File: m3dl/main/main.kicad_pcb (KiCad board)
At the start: 2 copper layers, 40 x 40 mm, 34 parts, among them IC1 STM32F405RxTx, IC2 MCP2562, J1 WEST TOP, J2 EAST TOP, J3 WEST BOT, J4 EAST BOT, J6 MICROUSB, J7 SOUTH TOP, P1 SWD_TC, U1 MICROSD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

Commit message: Finished Routing & Silk on all Boards
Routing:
- net (no net): vias 1 -> 0
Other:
- board text added: "C10"
- board text added: "C11"
- board text added: "C12"
- board text added: "C13"
- board text added: "C14"
- board text added: "C15"
- board text added: "C16"
- board text added: "C2"
- board text added: "C3"
- board text added: "C4"
- board text added: "C5"
- board text added: "C6"
- board text added: "C7"
- board text added: "C8"
- board text added: "C9"
- board text added: "R1"
- board text added: "R2"
- board text added: "R3"
- board text added: "R4"
- board text added: "R5"
- board text added: "R6"
- board text added: "R7"
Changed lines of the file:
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@@
     (area 79.725 77.094999 120.075001 120.075001)
     (thickness 1.6)
-    (drawings 2)
-    (tracks 632)
+    (drawings 24)
+    (tracks 631)
     (zones 0)
     (modules 34)
@@
     (34 B.Paste user hide)
     (35 F.Paste user hide)
-    (36 B.SilkS user hide)
-    (37 F.SilkS user hide)
+    (36 B.SilkS user)
+    (37 F.SilkS user)
     (38 B.Mask user hide)
     (39 F.Mask user hide)
@@
   )
   (setup
-    (last_trace_width 0.28)
+    (last_trace_width 0.25)
     (user_trace_width 0.2)
     (user_trace_width 0.28)
@@
       (net 4 "Net-(C3-Pad2)"))
   )
-  (gr_text C1 (at 94.25 113.5) (layer F.SilkS)
-    (effects (font (size 0.5 0.5) (thickness 0.1)))
+  (gr_text C9 (at 108.2 102.7) (layer B.SilkS)
+    (effects (font (size 0.6 0.6) (thickness 0.12)) (justify mirror))
+  )
+  (gr_text C12 (at 104 100) (layer B.SilkS)
+    (effects (font (size 0.6 0.6) (thickness 0.12)) (justify mirror))
+  )
+  (gr_text R5 (at 97 99.7) (layer B.SilkS)
+    (effects (font (size 0.6 0.6) (thickness 0.12)) (justify mirror))
+  )
+  (gr_text R6 (at 97 101.3) (layer B.SilkS)
+    (effects (font (size 0.6 0.6) (thickness 0.12)) (justify mirror))
+  )
+  (gr_text R7 (at 97 103) (layer B.SilkS)
+    (effects (font (size 0.6 0.6) (thickness 0.12)) (justify mirror))
+  )
+  (gr_text C7 (at 102.3 108) (layer B.SilkS)
+    (effects (font (size 0.6 0.6) (thickness 0.12)) (justify mirror))
+  )
+  (gr_text C15 (at 99.5 108) (layer B.SilkS)
+    (effects (font (size 0.6 0.6) (thickness 0.12)) (justify mirror))
+  )
+  (gr_text C14 (at 95.6 108) (layer B.SilkS)
+    (effects (font (size 0.6 0.6) (thickness 0.12)) (justify mirror))
+  )
+  (gr_text C8 (at 93.7 108) (layer B.SilkS)
+    (effects (font (size 0.6 0.6) (thickness 0.12)) (justify mirror))
+  )
+  (gr_text C11 (at 91.9 108) (layer B.SilkS)
+    (effects (font (size 0.6 0.6) (thickness 0.12)) (justify mirror))
+  )
+  (gr_text C16 (at 89.5 114.1) (layer B.SilkS)
+    (effects (font (size 0.6 0.6) (thickness 0.12)) (justify mirror))
+  )
+  (gr_text C4 (at 110.4 97.4) (layer F.SilkS)
+    (effects (font (size 0.6 0.6) (thickness 0.12)))
+  )
+  (gr_text C13 (at 110.6 95.8) (layer F.SilkS)
+    (effects (font (size 0.6 0.6) (thickness 0.12)))
+  )
+  (gr_text C10 (at 110.6 94.2) (layer F.SilkS)
+    (effects (font (size 0.6 0.6) (thickness 0.12)))
+  )
+  (gr_text R3 (at 103.6 90) (layer F.SilkS)
+    (effects (font (size 0.6 0.6) (thickness 0.12)))
+  )
+  (gr_text R1 (at 101.5 90.1) (layer F.SilkS)
+    (effects (font (size 0.6 0.6) (thickness 0.12)))
+  )
+  (gr_text R4 (at 98.8 90.1) (layer F.SilkS)
+    (effects (font (size 0.6 0.6) (thickness 0.12)))
+  )
+  (gr_text C5 (at 97.3 89.7) (layer F.SilkS)
+    (effects (font (size 0.6 0.6) (thickness 0.12)))
+  )
+  (gr_text C6 (at 95.7 89.7) (layer F.SilkS)
+    (effects (font (size 0.6 0.6) (thickness 0.12)))
+  )
+  (gr_text C3 (at 96.1 109.8) (layer F.SilkS)
+    (effects (font (size 0.6 0.6) (thickness 0.12)))
+  )
+  (gr_text C2 (at 93.6 104.8) (layer F.SilkS)
+    (effects (font (size 0.6 0.6) (thickness 0.12)))
+  )
+  (gr_text R2 (at 98.5 108.6) (layer F.SilkS)
+    (effects (font (size 0.6 0.6) (thickness 0.12)))
+  )
+  (gr_text C1 (at 94.2 113.7) (layer F.SilkS)
+    (effects (font (size 0.6 0.6) (thickness 0.12)))
   )
   (gr_circle (center 100 100) (end 120 100) (layer Edge.Cuts) (width 0.15))
-  (via (at 95.9 98.5) (size 0.6) (drill 0.3) (layers F.Cu B.Cu) (net 0))
   (segment (start 103.565 97.765) (end 102.7 96.9) (width 0.25) (layer B.Cu) (net 1))
   (segment (start 102.7 96.9) (end 102.7 95.9) (width 0.25) (layer B.Cu) (net 1))

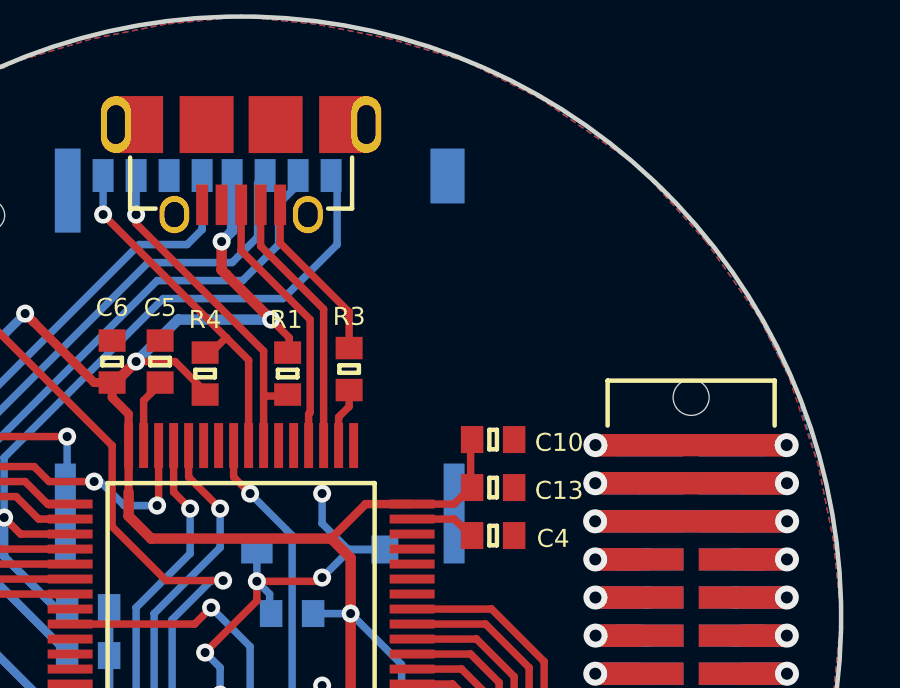
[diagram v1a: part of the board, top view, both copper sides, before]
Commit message: Addition of LEDs to Main
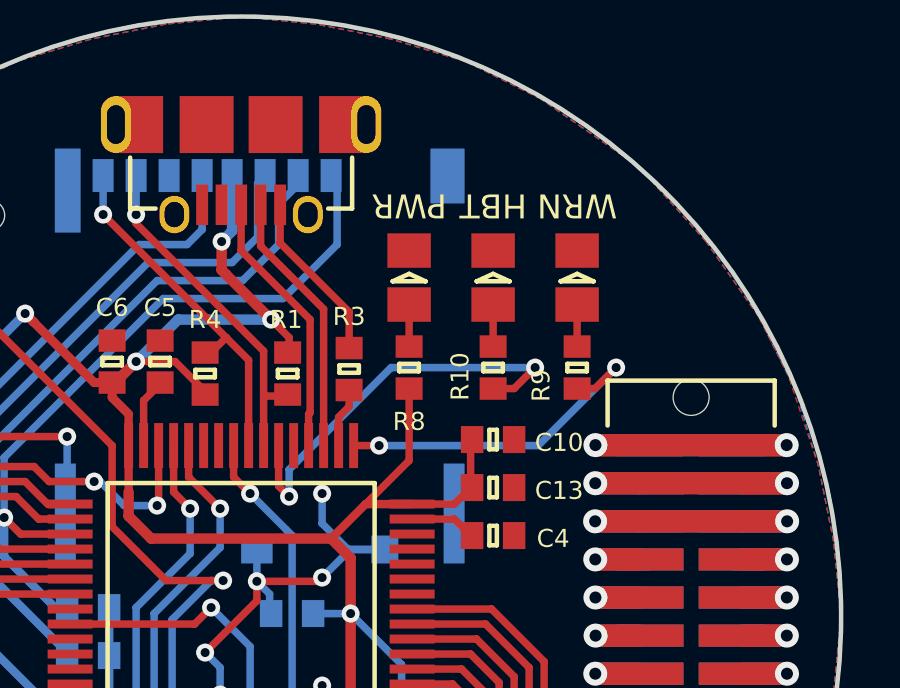
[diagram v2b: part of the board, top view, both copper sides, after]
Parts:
- added D1: LED, agg:0805-LED, F.Cu at (105.6, 88.7)
- added D2: LED, agg:0805-LED, F.Cu at (111.2, 88.7)
- added D3: LED, agg:0805-LED, F.Cu at (108.4, 88.7)
- added R10: 1k, agg:0603-L, F.Cu at (108.4, 91.7)
- added R8: 1k, agg:0603-L, F.Cu at (105.6, 91.7)
- added R9: 1k, agg:0603-L, F.Cu at (111.2, 91.7)
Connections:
- IC1 pad 33: Net-(IC1-Pad33) -> /LED1
- IC1 pad 38: Net-(IC1-Pad38) -> /LED2
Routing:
- net /LED2: track 0.00 -> 14.0 mm, vias 0 -> 2
- net /LED1: track 0.00 -> 11.4 mm, vias 0 -> 2
- net 3v3: track 110.9 -> 115.3 mm
- net Net-(D3-Pad2): track 0.00 -> 1.40 mm
- net Net-(D2-Pad2): track 0.00 -> 1.40 mm
- net Net-(D1-Pad2): track 0.00 -> 1.40 mm
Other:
- board text added: "HBT"
- board text added: "PWR"
- board text added: "R10"
- board text added: "R8"
- board text added: "R9"
- board text added: "WRN"

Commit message: Almost ready to generate gerbers
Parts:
- J6: value MICROUSB -> USB; footprint agg:MICROUSB_MOLEX_47589-0001 -> Connectors_Molex:Connector_Molex_PicoBlade_53261-0471
- moved J6 0.52 mm to (99.9, 83.1)
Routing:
- net 3v3: track 115.3 -> 118.4 mm
- net /SDIO_CK: track 21.3 -> 20.2 mm
- net /TEMP_INT: track 23.4 -> 24.2 mm
- net /OTG_HS_DP: track 9.00 -> 9.58 mm
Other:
- net class Default: clearance 0.1 -> 0.127; trace_width 0.25 -> 0.2
- rule pad_to_mask_clearance: 0.2 -> 0
- rule trace_clearance: 0.1 -> 0.127
- board text added: "SWD"
- board text added: "USB"

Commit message: All finished except logos
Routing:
- net GND: track 113.4 -> 227.7 mm, vias 19 -> 59

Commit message: All PCBs Finished
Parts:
- added G***: LOGO, logos:cusf_logo_full, F.Cu at (109.7, 112.6)
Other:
- board text added: "m3dl - Main Matt Coates 11/03/16"

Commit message: Uploaded Gerbers
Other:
- board text added: "m3dl - Main r1 Matt Coates 11/03/16"
- board text removed: "m3dl - Main Matt Coates 11/03/16"
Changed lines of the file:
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@@
     (pcbplotparams
       (layerselection 0x010f0_80000001)
-      (usegerberextensions false)
+      (usegerberextensions true)
       (excludeedgelayer true)
       (linewidth 0.100000)
@@
       (plotinvisibletext false)
       (padsonsilk false)
-      (subtractmaskfromsilk false)
+      (subtractmaskfromsilk true)
       (outputformat 1)
       (mirror false)
       (drillshape 0)
       (scaleselection 1)
-      (outputdirectory ""))
+      (outputdirectory gerbers/))
   )
   (net 0 "")
@@
       (xy 5.4229 -3.5433)) (layer F.SilkS) (width 0.01))
   )
-  (gr_text "m3dl - Main\nMatt Coates\n11/03/16" (at 114.4 110.65) (layer B.SilkS)
+  (gr_text "m3dl - Main r1\nMatt Coates\n11/03/16" (at 114.4 110.65) (layer B.SilkS)
     (effects (font (size 0.7 0.7) (thickness 0.1)) (justify left mirror))
   )

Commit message: Modifications as per review document
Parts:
- removed C11: 100n, agg:0603-L
- C10: value 1u -> 4u7
- C12: moved to F.Cu
- C2, C3: value 18p -> 10p
- C6: value 10n -> 100n
- J7: value SOUTH TOP -> SOUTH BOT
- Y1: value 8MHz -> 26MHz
- moved C12 11.8 mm to (98.4, 88.6), turned to 225 degrees
- moved G*** 0.76 mm to (109.0, 113.0)
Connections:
- net /5V_CAN renamed /5v_CAN
- IC1 pad 44: /CAN_RXD -> Net-(IC1-Pad44)
- IC1 pad 45: /CAN_TXD -> Net-(IC1-Pad45)
- IC1 pad 57: /TEMP_INT -> /CAN_RXD
- IC1 pad 58: Net-(IC1-Pad58) -> /CAN_TXD
- IC1 pad 59: Net-(IC1-Pad59) -> /TEMP_INT
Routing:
- net 3v3: track 118.4 -> 112.2 mm
- net GND: track 228.2 -> 232.9 mm, vias 59 -> 61
- net /CAN_TXD: track 25.4 -> 20.7 mm
- net /CAN_RXD: track 24.0 -> 21.2 mm
- net /SDIO_D1: track 11.9 -> 11.1 mm
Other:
- net class Default: clearance 0.127 -> 0.15
- rule trace_clearance: 0.127 -> 0.15
- board text removed: "C11"

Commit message: Generated gerbers
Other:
- board text added: "m3dl - Main r1 Matt Coates 12/06/16"
- board text removed: "m3dl - Main r1 Matt Coates 11/03/16"
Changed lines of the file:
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@@
       (xy 5.4229 -3.5433)) (layer F.SilkS) (width 0.01))
   )
-  (gr_text "m3dl - Main r1\nMatt Coates\n11/03/16" (at 114.4 110.65) (layer B.SilkS)
+  (gr_text "m3dl - Main r1\nMatt Coates\n12/06/16" (at 114.4 110.65) (layer B.SilkS)
     (effects (font (size 0.7 0.7) (thickness 0.1)) (justify left mirror))
   )
